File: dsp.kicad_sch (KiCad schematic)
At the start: 54 parts, among them J3 pots, J4 Conn_01x04, Q1 Q_PNP_BCE, U15 Opamp_Dual, U16 Opamp_Dual, U22 ADAU1701, U23 MC33275, U24 MC33275

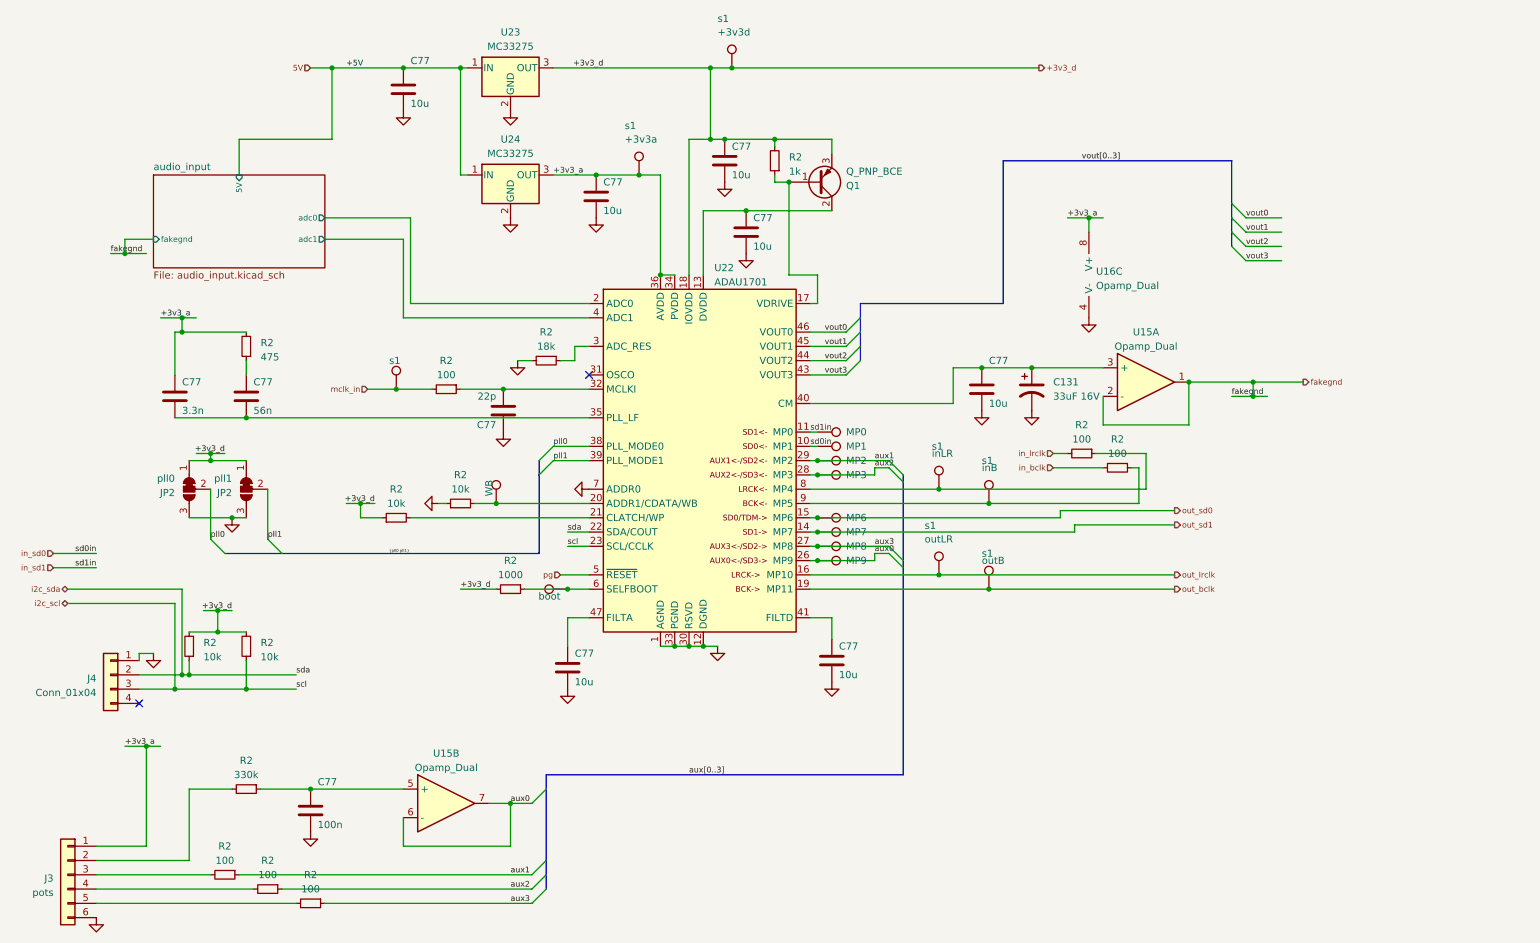
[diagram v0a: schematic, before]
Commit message: update to kicad 8
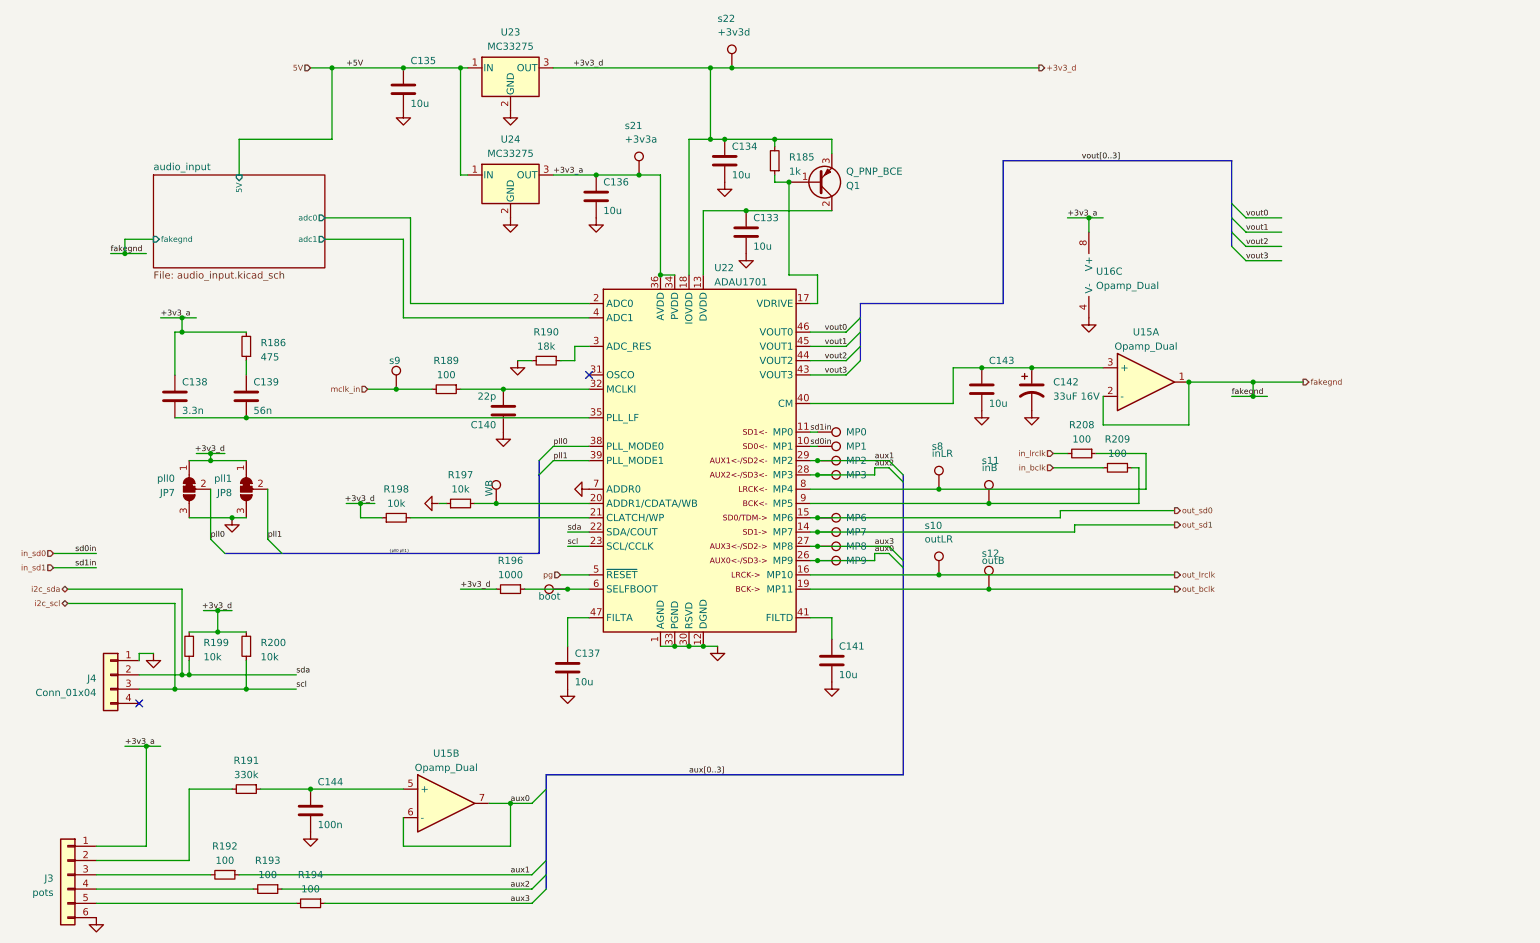
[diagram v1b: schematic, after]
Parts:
- renumbered C77 to C133, C77 to C134, C77 to C135, C77 to C136, C77 to C137, C77 to C138, C77 to C139, C77 to C140, C77 to C141, C131 to C142, C77 to C143, C77 to C144, JP2 to JP7, JP2 to JP8, R2 to R185, R2 to R186, R2 to R189, R2 to R190, R2 to R191, R2 to R192, R2 to R193, R2 to R194, R2 to R196, R2 to R197, R2 to R198, R2 to R199, R2 to R200, R2 to R208, R2 to R209, s1 to s10, s1 to s11, s1 to s12, s1 to s13, s1 to s14, s1 to s15, s1 to s16, s1 to s17, s1 to s18, s1 to s19, s1 to s20, s1 to s21, s1 to s22, s1 to s26, s1 to s27, s1 to s8, s1 to s9

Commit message: schematic: some fixes
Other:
- added sheet line_out (line_out.kicad_sch)
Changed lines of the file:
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@@
+	)
+	(sheet
+		(at 240.03 41.91)
+		(size 35.56 20.32)
+		(fields_autoplaced yes)
+		(stroke
+			(width 0.1524)
+			(type solid)
+		)
+		(fill
+			(color 0 0 0 0.0000)
+		)
+		(property "Sheetname" "line_out"
+			(at 240.03 41.1984 0)
+			(effects
+				(font
+					(size 1.27 1.27)
+				)
+				(justify left bottom)
+			)
+		)
+		(property "Sheetfile" "line_out.kicad_sch"
+			(at 240.03 62.8146 0)
+			(effects
+				(font
+					(size 1.27 1.27)
+				)
+				(justify left top)
+			)
+		)
+		(instances
+			(project "uberamp1"
+				(path "/310059c1-d84b-43e2-9c9a-0e426c534a12/9f0654db-0c52-4f70-8768-bb44a6ed6168"
+					(page "21")
+				)
+			)
+		)
 	)
 	(sheet

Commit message: updates
* add line out
* fix almost all erc
* some more random edits
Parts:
- U23, U24: PN (none) -> MC33275ST
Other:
- sheet line_out ports: added 5V, en, input_ref, s0, s1, s2, s3; removed none

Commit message: add power input +...
+ tons of fixes, footprint assignments, etc
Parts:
- added CU16: 10u, invendelirium_audio:C_0603, symbol Device:C
- U15, U16: footprint (none) -> invendelirium_audio:SOIC-8
- U22: PN (none) -> adau1701
- U23, U24: PN MC33275ST -> MC33275ST-3.3
- renumbered C134 to CU22, C135 to CU23
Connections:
- net +3v3_a: now also CU16.1
- net GND: now also CU16.2

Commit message: fix gate association U15 U16
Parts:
- renumbered U16 to U15
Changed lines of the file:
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@@
 		(dnp no)
 		(fields_autoplaced yes)
-		(property "Reference" "U16"
+		(property "Reference" "U15"
 			(at 205.74 57.785 0)
 			(effects
@@
 			(project "uberamp1"
 				(path "/310059c1-d84b-43e2-9c9a-0e426c534a12/9f0654db-0c52-4f70-8768-bb44a6ed6168"
-					(reference "U16")
+					(reference "U15")
 					(unit 3)
 				)

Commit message: routing routing...
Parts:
- added C78, C82: 10u, invendelirium_audio:C_0603, symbol Device:C
- Q1: footprint PCM_4ms_Package_SOT:SOT23-3_PO123 -> invendelirium_general:SOT23-3_PO123
- U23, U24: footprint Package_TO_SOT_SMD:SOT-223-3_TabPin2 -> invendelirium_general:SOT-223-3_TabPin2
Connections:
- net +3v3_a: now also JP7.1 (A), JP8.1 (A), C78.1
- net +3v3_d: no longer JP7.1 (A), JP8.1 (A)
- net GND: now also C78.2, C82.2
- net at C133.1, Q1.2 (C), U22.13 (DVDD)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: now also C82.1
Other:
- note added: "because layout was easier"
- moved on the sheet: C133

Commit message: lots of drc-related work
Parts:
- removed R199, R200: 10k, invendelirium_audio:R_0603, symbol Device:R_Small
- added CU30: 10u, invendelirium_audio:C_0603, symbol Device:C
- added U30: M24128 (128kbit), invendelirium_general:TSSOP-8_STM, symbol Memory_EEPROM:AT24CS01-XHM
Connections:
- net +3v3_d: now also CU30.1, U30.8 (VCC)
- net GND: now also CU30.2, U30.1 (A0), U30.2 (A1), U30.3 (A2), U30.4 (GND), U30.7 (WP)
- net i2c_scl: now also U30.6 (SCL)
- net i2c_sda: now also U30.5 (SDA)

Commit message: fill in some part numbers
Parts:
- JP7, JP8, s10, s11, s12, s13, s14, s15, s16, s17, s18, s19, s20, s21, s22, s26, s27, s8, s9: now left out of the parts list
- R190: PN (none) -> RT0603DRD0718KL
- U15: PN (none) -> OPA2322AIDR
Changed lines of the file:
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@@
 			)
 		)
+		(property "PN" "RT0603DRD0718KL"
+			(at 107.95 73.66 0)
+			(effects
+				(font
+					(size 1.27 1.27)
+				)
+				(hide yes)
+			)
+		)
 		(pin "1"
 		)
@@
 			)
 		)
+		(property "PN" "OPA2322AIDR"
+			(at 207.01 58.42 0)
+			(effects
+				(font
+					(size 1.27 1.27)
+				)
+				(hide yes)
+			)
+		)
 		(pin "1"
 		)
@@
 		(unit 1)
 		(exclude_from_sim no)
-		(in_bom yes)
+		(in_bom no)
 		(on_board yes)
 		(dnp no)
@@
 		(unit 1)
 		(exclude_from_sim no)
-		(in_bom yes)
+		(in_bom no)
 		(on_board yes)
 		(dnp no)
@@
 			)
 		)
+		(property "PN" "OPA2322AIDR"
+			(at 90.17 152.4 0)
+			(effects
+				(font
+					(size 1.27 1.27)
+				)
+				(hide yes)
+			)
+		)
 		(pin "1"
 		)
@@
 		(unit 1)
 		(exclude_from_sim no)
-		(in_bom yes)
+		(in_bom no)
 		(on_board yes)
 		(dnp no)
@@
 			)
 		)
+		(property "PN" "OPA2322AIDR"
+			(at 214.63 77.47 0)
+			(effects
+				(font
+					(size 1.27 1.27)
+				)
+				(hide yes)
+			)
+		)
 		(pin "1"
 		)
@@
 		(unit 1)
 		(exclude_from_sim no)
-		(in_bom yes)
+		(in_bom no)
 		(on_board yes)
 		(dnp no)
@@
 		(unit 1)
 		(exclude_from_sim no)
-		(in_bom yes)
+		(in_bom no)
 		(on_board yes)
 		(dnp no)
@@
 		(unit 1)
 		(exclude_from_sim no)
-		(in_bom yes)
+		(in_bom no)
 		(on_board yes)
 		(dnp no)
@@
 		(unit 1)
 		(exclude_from_sim no)
-		(in_bom yes)
+		(in_bom no)
 		(on_board yes)
 		(dnp no)
@@
 		(unit 1)
 		(exclude_from_sim no)
-		(in_bom yes)
+		(in_bom no)
 		(on_board yes)
 		(dnp no)
@@
 		(unit 1)
 		(exclude_from_sim no)
-		(in_bom yes)
+		(in_bom no)
 		(on_board yes)
 		(dnp no)
@@
 		(unit 1)
 		(exclude_from_sim no)
-		(in_bom yes)
+		(in_bom no)
 		(on_board yes)
 		(dnp no)
@@
 		(unit 1)
 		(exclude_from_sim no)
-		(in_bom yes)
+		(in_bom no)
 		(on_board yes)
 		(dnp no)
@@
 		(unit 1)
 		(exclude_from_sim no)
-		(in_bom yes)
+		(in_bom no)
 		(on_board yes)
 		(dnp no)
@@
 		(unit 1)
 		(exclude_from_sim no)
-		(in_bom yes)
+		(in_bom no)
 		(on_board yes)
 		(dnp no)
@@
 		(unit 1)
 		(exclude_from_sim no)
-		(in_bom yes)
+		(in_bom no)
 		(on_board yes)
 		(dnp no)
@@
 		(unit 1)
 		(exclude_from_sim no)
-		(in_bom yes)
+		(in_bom no)
 		(on_board yes)
 		(dnp no)
@@
 		(unit 1)
 		(exclude_from_sim no)
-		(in_bom yes)
+		(in_bom no)
 		(on_board yes)
 		(dnp no)
@@
 		(unit 1)
 		(exclude_from_sim no)
-		(in_bom yes)
+		(in_bom no)
 		(on_board yes)
 		(dnp no)
@@
 		(unit 1)
 		(exclude_from_sim no)
-		(in_bom yes)
+		(in_bom no)
 		(on_board yes)
 		(dnp no)
@@
 		(unit 1)
 		(exclude_from_sim no)
-		(in_bom yes)
+		(in_bom no)
 		(on_board yes)
 		(dnp no)
